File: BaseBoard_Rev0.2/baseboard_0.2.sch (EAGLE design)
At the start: 118 parts, among them Q1 IRLML5203, Q2 IRLML5203, Q3 PDTC114E, Q4 PDTC114E, Q5 PDTC114E, U3 NCP3337MNADJR2G, U4 NCP3337MNADJR2G, X1 CRYSTAL_212M_

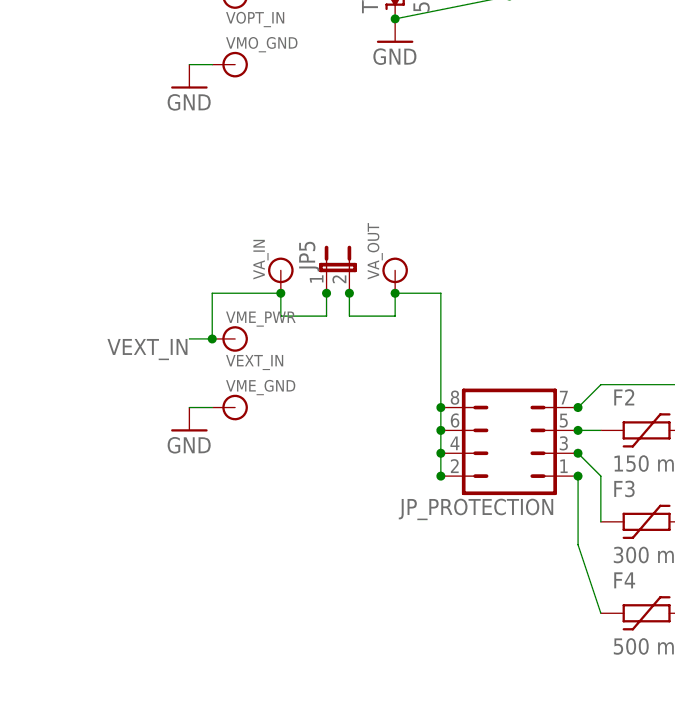
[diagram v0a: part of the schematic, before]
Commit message: Added shunt resistor for current measurement
In case of no ammeter
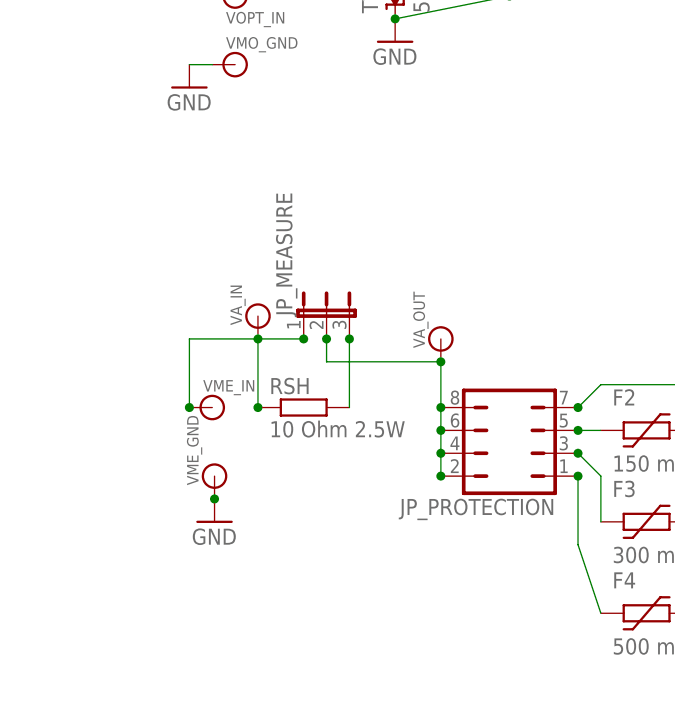
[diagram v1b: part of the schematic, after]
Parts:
- removed JP5: (no value), SparkFun-Passives:JUMPER-2PTH
- removed VME_PWR: VEXT_IN, SparkFun-Connectors:BANANA_CONN
- added JP_MEASURE: (no value), jumper:JP2E
- added RSH: 10 Ohm 2.5W, rcl:R-EU_R2512
- added VME_IN: (no value), SparkFun-Connectors:BANANA_CONN
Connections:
- new net N$33: JP_MEASURE.1, RSH.1, VA_IN.1, VME_IN.1
- new net N$35: JP_MEASURE.3, RSH.2
- net VEXT_IN: now also JP_MEASURE.2; no longer JP5.1, JP5.2, VA_IN.1, VME_PWR.1
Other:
- moved on the sheet: VA_IN, VA_OUT, VME_GND
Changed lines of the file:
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@@
 <layer number="97" name="Info" color="7" fill="1" visible="yes" active="yes"/>
 <layer number="98" name="Guide" color="6" fill="1" visible="yes" active="yes"/>
+<layer number="99" name="SpiceOrder" color="5" fill="1" visible="yes" active="yes"/>
 <layer number="100" name="Muster" color="7" fill="1" visible="no" active="no"/>
 <layer number="101" name="Patch_Top" color="12" fill="4" visible="yes" active="yes"/>
@@
 <part name="3.3V19" library="supply1" deviceset="+3V3" device="" value="3.3V"/>
 <part name="VA_IN" library="SparkFun-Connectors" deviceset="BANANA_CONN" device=""/>
-<part name="VA_OUT" library="SparkFun-Connectors" deviceset="BANANA_CONN" device=""/>
-<part name="JP5" library="SparkFun-Passives" deviceset="JUMPER-2" device="PTH"/>
-<part name="VME_PWR" library="SparkFun-Connectors" deviceset="BANANA_CONN" device="" value="VEXT_IN"/>
 <part name="VME_GND" library="SparkFun-Connectors" deviceset="BANANA_CONN" device=""/>
 <part name="GND6" library="supply1" deviceset="GND" device=""/>
@@
 <part name="JP8" library="pinhead" deviceset="PINHD-1X3" device=""/>
 <part name="JP6" library="pinhead" deviceset="PINHD-1X3" device=""/>
+<part name="RSH" library="rcl" deviceset="R-EU_" device="R2512" value="10 Ohm 2.5W"/>
+<part name="VA_OUT" library="SparkFun-Connectors" deviceset="BANANA_CONN" device=""/>
+<part name="VME_IN" library="SparkFun-Connectors" deviceset="BANANA_CONN" device=""/>
+<part name="JP_MEASURE" library="jumper" deviceset="JP2E" device=""/>
 </parts>
 <sheets>
@@
 <attribute name="VALUE" x="434.34" y="322.58" size="1.778" layer="96"/>
 </instance>
-<instance part="VA_IN" gate="G$1" x="27.94" y="152.4" rot="R90"/>
-<instance part="VA_OUT" gate="G$1" x="40.64" y="152.4" rot="R90"/>
-<instance part="JP5" gate="A" x="33.02" y="152.4"/>
-<instance part="VME_PWR" gate="G$1" x="22.86" y="144.78"/>
-<instance part="VME_GND" gate="G$1" x="22.86" y="137.16"/>
-<instance part="GND6" gate="1" x="17.78" y="134.62"/>
+<instance part="VA_IN" gate="G$1" x="25.4" y="147.32" rot="R90"/>
+<instance part="VME_GND" gate="G$1" x="20.574" y="129.54" rot="R90"/>
+<instance part="GND6" gate="1" x="20.574" y="124.46"/>
 <instance part="VMO_GND" gate="G$1" x="22.86" y="175.26"/>
 <instance part="GND8" gate="1" x="17.78" y="172.72"/>
@@
 <instance part="JP8" gate="A" x="170.18" y="121.92"/>
 <instance part="JP6" gate="A" x="198.12" y="121.92"/>
+<instance part="RSH" gate="G$1" x="30.48" y="137.16"/>
+<instance part="VA_OUT" gate="G$1" x="45.72" y="144.78" rot="R90"/>
+<instance part="VME_IN" gate="G$1" x="20.32" y="137.16"/>
+<instance part="JP_MEASURE" gate="1" x="33.02" y="147.32"/>
 </instances>
 <busses>
@@
 <segment>
 <pinref part="VME_GND" gate="G$1" pin="1"/>
-<wire x1="20.32" y1="137.16" x2="17.78" y2="137.16" width="0.1524" layer="91"/>
 <pinref part="GND6" gate="1" pin="GND"/>
+<junction x="20.574" y="127"/>
 </segment>
 <segment>
@@
 <net name="VEXT_IN" class="0">
 <segment>
-<pinref part="JP5" gate="A" pin="2"/>
-<wire x1="35.56" y1="149.86" x2="35.56" y2="147.32" width="0.1524" layer="91"/>
-<pinref part="VA_OUT" gate="G$1" pin="1"/>
-<wire x1="40.64" y1="149.86" x2="40.64" y2="147.32" width="0.1524" layer="91"/>
-<wire x1="40.64" y1="147.32" x2="35.56" y2="147.32" width="0.1524" layer="91"/>
 <pinref part="JP_PROTECTION" gate="B" pin="2"/>
 <pinref part="JP_PROTECTION" gate="B" pin="4"/>
@@
 <wire x1="45.72" y1="132.08" x2="45.72" y2="129.54" width="0.1524" layer="91"/>
 <junction x="45.72" y="129.54"/>
-<wire x1="45.72" y1="137.16" x2="45.72" y2="149.86" width="0.1524" layer="91"/>
-<wire x1="45.72" y1="149.86" x2="40.64" y2="149.86" width="0.1524" layer="91"/>
-<junction x="40.64" y="149.86"/>
-<junction x="35.56" y="149.86"/>
+<wire x1="45.72" y1="137.16" x2="45.72" y2="142.24" width="0.1524" layer="91"/>
 <junction x="45.72" y="137.16"/>
-</segment>
-<segment>
-<pinref part="VME_PWR" gate="G$1" pin="1"/>
-<wire x1="20.32" y1="144.78" x2="17.78" y2="144.78" width="0.1524" layer="91"/>
-<wire x1="20.32" y1="144.78" x2="20.32" y2="149.86" width="0.1524" layer="91"/>
-<pinref part="VA_IN" gate="G$1" pin="1"/>
-<wire x1="27.94" y1="149.86" x2="27.94" y2="147.32" width="0.1524" layer="91"/>
-<wire x1="27.94" y1="147.32" x2="33.02" y2="147.32" width="0.1524" layer="91"/>
-<pinref part="JP5" gate="A" pin="1"/>
-<wire x1="33.02" y1="147.32" x2="33.02" y2="149.86" width="0.1524" layer="91"/>
-<wire x1="20.32" y1="149.86" x2="27.94" y2="149.86" width="0.1524" layer="91"/>
-<junction x="27.94" y="149.86"/>
-<label x="17.78" y="144.78" size="1.778" layer="95" rot="R180"/>
-<junction x="20.32" y="144.78"/>
-<junction x="33.02" y="149.86"/>
+<pinref part="VA_OUT" gate="G$1" pin="1"/>
+<pinref part="JP_MEASURE" gate="1" pin="2"/>
+<wire x1="33.02" y1="144.78" x2="33.02" y2="142.24" width="0.1524" layer="91"/>
+<wire x1="33.02" y1="142.24" x2="45.72" y2="142.24" width="0.1524" layer="91"/>
+<junction x="45.72" y="142.24"/>
+<junction x="33.02" y="144.78"/>
 </segment>
 </net>
@@
 <net name="V_CPU" class="0">
 <segment>
-<pinref part="TARGET_SW" gate="G$1" pin="1"/>
-<wire x1="233.68" y1="119.38" x2="251.46" y2="119.38" width="0.1524" layer="91"/>
-<label x="241.3" y="119.38" size="1.778" layer="95"/>
-</segment>
-<segment>
 <pinref part="JP10" gate="A" pin="1"/>
 <label x="22.86" y="81.28" size="1.27" layer="95" rot="R180" xref="yes"/>
@@
 <pinref part="JP11" gate="G$1" pin="1"/>
 <junction x="41.91" y="81.28"/>
+</segment>
+<segment>
+<pinref part="TARGET_SW" gate="G$1" pin="1"/>
+<wire x1="233.68" y1="119.38" x2="251.46" y2="119.38" width="0.1524" layer="91"/>
+<label x="241.3" y="119.38" size="1.778" layer="95"/>
 </segment>
 </net>
@@
 </segment>
 </net>
+<net name="N$33" class="0">
+<segment>
+<pinref part="VA_IN" gate="G$1" pin="1"/>
+<wire x1="25.4" y1="137.16" x2="25.4" y2="144.78" width="0.1524" layer="91"/>
+<pinref part="RSH" gate="G$1" pin="1"/>
+<junction x="25.4" y="137.16"/>
+<pinref part="JP_MEASURE" gate="1" pin="1"/>
+<wire x1="30.48" y1="144.78" x2="25.4" y2="144.78" width="0.1524" layer="91"/>
+<wire x1="17.78" y1="137.16" x2="17.78" y2="144.78" width="0.1524" layer="91"/>
+<wire x1="17.78" y1="144.78" x2="25.4" y2="144.78" width="0.1524" layer="91"/>
+<junction x="25.4" y="144.78"/>
+<junction x="30.48" y="144.78"/>
+<pinref part="VME_IN" gate="G$1" pin="1"/>
+<junction x="17.78" y="137.16"/>
+</segment>
+</net>
+<net name="N$35" class="0">
+<segment>
+<pinref part="JP_MEASURE" gate="1" pin="3"/>
+<pinref part="RSH" gate="G$1" pin="2"/>
+<wire x1="35.56" y1="144.78" x2="35.56" y2="137.16" width="0.1524" layer="91"/>
+<junction x="35.56" y="144.78"/>
+</segment>
+</net>
